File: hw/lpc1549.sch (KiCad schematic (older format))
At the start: 20 parts, among them J301 ARM_JTAG_SWD_HEADER_10_PINSMD, U301 LPC1549JBD64, U302 MCP2551_SOIC8, X301 XTAL_7A-12.000MAAJ-T

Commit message: creating hw 3.0.0
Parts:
- removed R301, R304, R305, R307: 10K, multicomp:0603, symbol 10K
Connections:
- net EMCY: now also U301.P$41 (VBAT)
- net KEY_19: now also U301.P$33 (PIO1_4/ADC1_10)
- net KEY_50: now also U301.P$39 (PIO0_17/WAKEUP/!TRST)
- net KEY_AC: now also U301.P$34 (PIO1_5/ADC1_11)
- net HEATERBAT renamed HEATER
- net HEATERBAT_SENSE: no longer names the net of U301.P$8 (PIO0_4/ADC0_4)
- net HEATERVDD: no longer names the net of U301.P$30 (PIO0_14/ADC1_7/SCT1_OUT5)
- net HEATERVDD_SENSE renamed HEATER_SENSE
- net OUT4: no longer names the net of U301.P$64 (PIO0_29/ACMP2_I3/SCT2_OUT4)
- net OUT4_SENSE: no longer names the net of U301.P$2 (PIO0_0/ADC0_10/SCT0_OUT3)

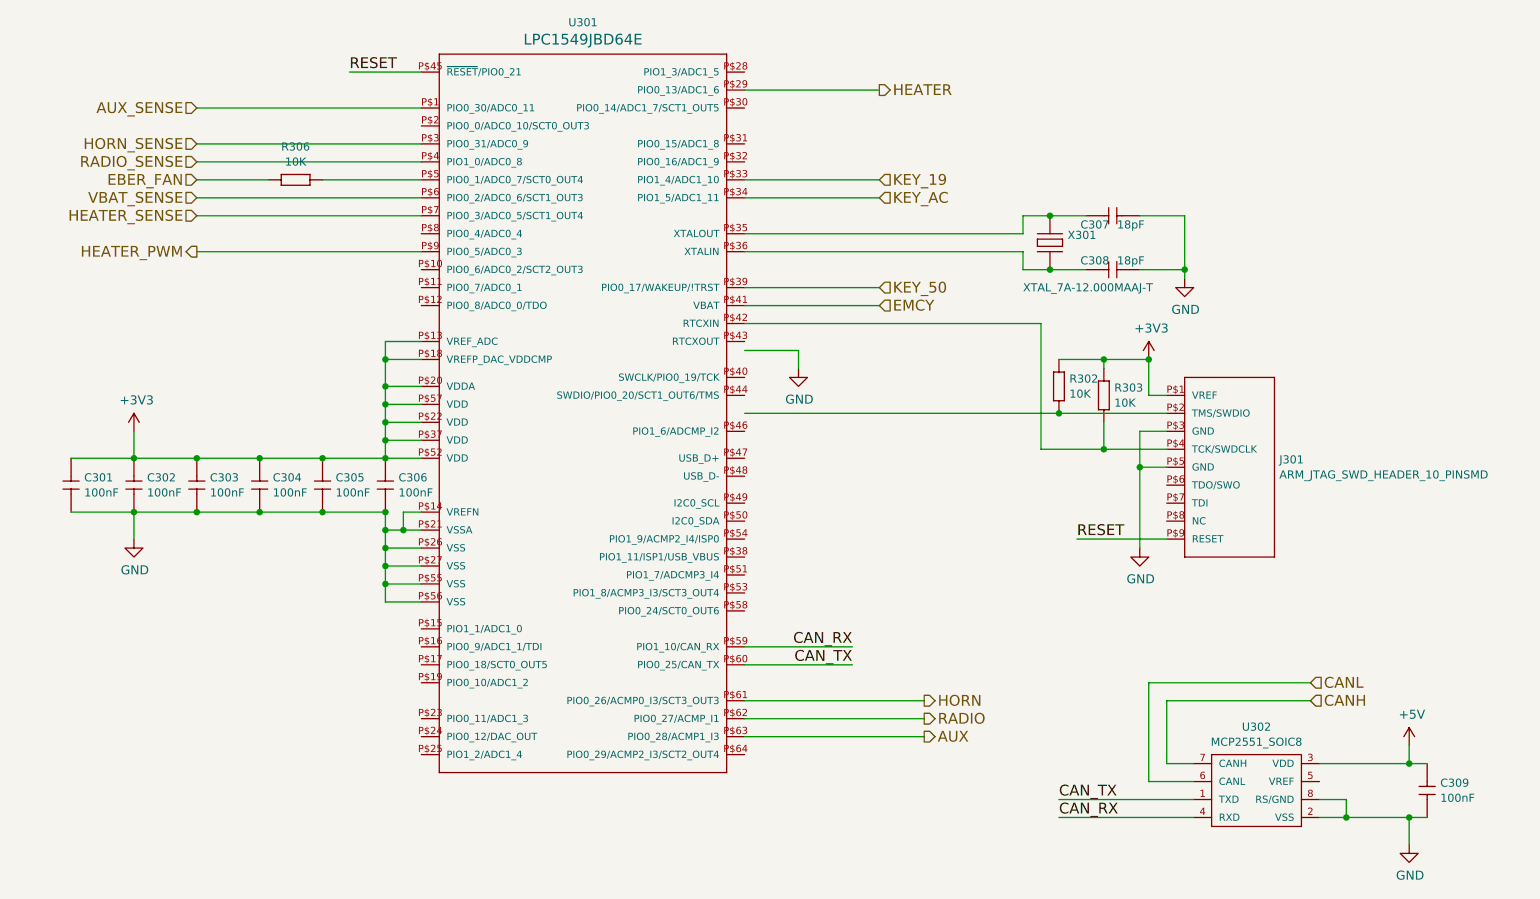
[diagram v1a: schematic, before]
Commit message: key_50 moved out from ISP pin
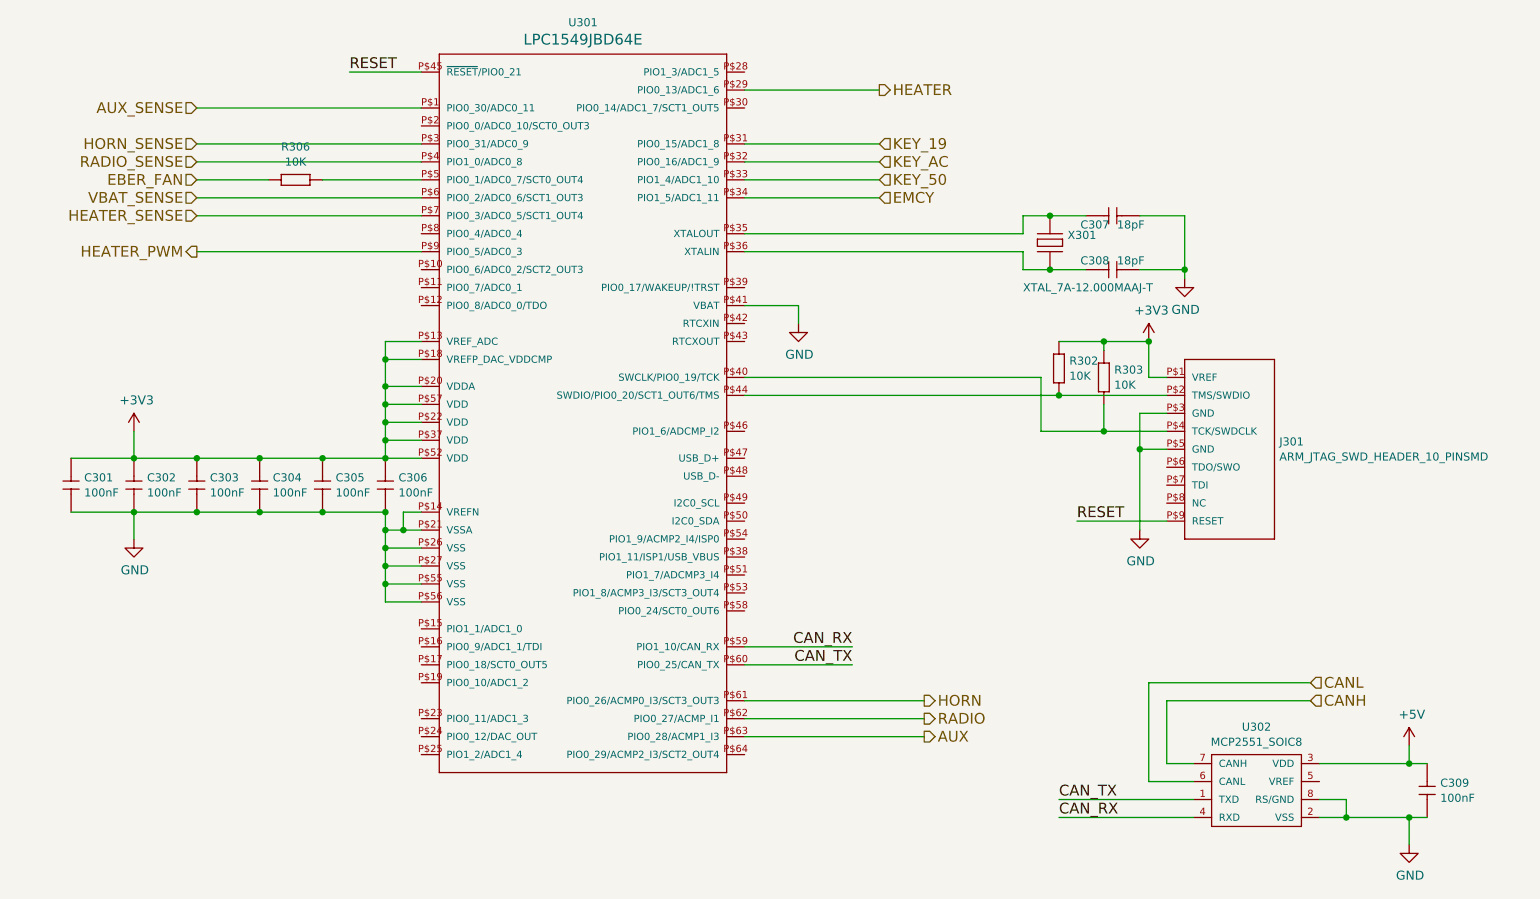
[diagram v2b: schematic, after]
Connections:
- net EMCY: now also U301.P$34 (PIO1_5/ADC1_11); no longer U301.P$41 (VBAT)
- net GND: now also U301.P$41 (VBAT)
- net KEY_19: now also U301.P$31 (PIO0_15/ADC1_8); no longer U301.P$33 (PIO1_4/ADC1_10)
- net KEY_50: now also U301.P$33 (PIO1_4/ADC1_10); no longer U301.P$39 (PIO0_17/WAKEUP/!TRST)
- net KEY_AC: now also U301.P$32 (PIO0_16/ADC1_9); no longer U301.P$34 (PIO1_5/ADC1_11)
- net at J301.P$2 (TMS/SWDIO), R302.1 (R1): now also U301.P$44 (SWDIO/PIO0_20/SCT1_OUT6/TMS)
- net at J301.P$4 (TCK/SWDCLK), R303.1 (R1): now also U301.P$40 (SWCLK/PIO0_19/TCK); no longer U301.P$42 (RTCXIN)
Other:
- moved on the sheet: J301, R302, R303
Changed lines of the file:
@@
 $EndComp
 $Comp
-L +3V3 #PWR301
+L +3V3 #PWR016
 U 1 1 57E689A3
 P 3000 3850
-F 0 "#PWR301" H 3000 3700 50  0001 C CNN
+F 0 "#PWR016" H 3000 3700 50  0001 C CNN
 F 1 "+3V3" H 3015 4023 50  0000 C CNN
 F 2 "" H 3000 3850 50  0000 C CNN
@@
 $EndComp
 $Comp
-L GND #PWR302
+L GND #PWR017
 U 1 1 57E689C9
 P 3000 4450
-F 0 "#PWR302" H 3000 4200 50  0001 C CNN
+F 0 "#PWR017" H 3000 4200 50  0001 C CNN
 F 1 "GND" H 3005 4277 50  0000 C CNN
 F 2 "" H 3000 4450 50  0000 C CNN
@@
 $EndComp
 $Comp
-L GND #PWR306
+L GND #PWR018
 U 1 1 57E697A1
 P 8850 3000
-F 0 "#PWR306" H 8850 2750 50  0001 C CNN
+F 0 "#PWR018" H 8850 2750 50  0001 C CNN
 F 1 "GND" H 8855 2827 50  0000 C CNN
 F 2 "" H 8850 3000 50  0000 C CNN
@@
 $EndComp
 $Comp
-L GND #PWR303
+L GND #PWR019
 U 1 1 57E69A8B
-P 6700 3500
-F 0 "#PWR303" H 6700 3250 50  0001 C CNN
-F 1 "GND" H 6705 3327 50  0000 C CNN
-F 2 "" H 6700 3500 50  0000 C CNN
-F 3 "" H 6700 3500 50  0000 C CNN
-	1    6700 3500
-	1    0    0    -1
-$EndComp
-$Comp
-L GND #PWR304
+P 6700 3250
+F 0 "#PWR019" H 6700 3000 50  0001 C CNN
+F 1 "GND" H 6705 3077 50  0000 C CNN
+F 2 "" H 6700 3250 50  0000 C CNN
+F 3 "" H 6700 3250 50  0000 C CNN
+	1    6700 3250
+	1    0    0    -1
+$EndComp
+$Comp
+L GND #PWR020
 U 1 1 5891FBFB
-P 8600 4500
-F 0 "#PWR304" H 8600 4250 50  0001 C CNN
-F 1 "GND" H 8605 4327 50  0000 C CNN
-F 2 "" H 8600 4500 50  0000 C CNN
-F 3 "" H 8600 4500 50  0000 C CNN
-	1    8600 4500
-	1    0    0    -1
-$EndComp
-$Comp
-L +3V3 #PWR305
+P 8600 4400
+F 0 "#PWR020" H 8600 4150 50  0001 C CNN
+F 1 "GND" H 8605 4227 50  0000 C CNN
+F 2 "" H 8600 4400 50  0000 C CNN
+F 3 "" H 8600 4400 50  0000 C CNN
+	1    8600 4400
+	1    0    0    -1
+$EndComp
+$Comp
+L +3V3 #PWR021
 U 1 1 5891FCDE
-P 8650 3450
-F 0 "#PWR305" H 8650 3300 50  0001 C CNN
-F 1 "+3V3" H 8665 3623 50  0000 C CNN
-F 2 "" H 8650 3450 50  0000 C CNN
-F 3 "" H 8650 3450 50  0000 C CNN
-	1    8650 3450
-	1    0    0    -1
-$EndComp
-Text Label 8250 4450 0    60   ~ 0
+P 8650 3350
+F 0 "#PWR021" H 8650 3200 50  0001 C CNN
+F 1 "+3V3" H 8665 3523 50  0000 C CNN
+F 2 "" H 8650 3350 50  0000 C CNN
+F 3 "" H 8650 3350 50  0000 C CNN
+	1    8650 3350
+	1    0    0    -1
+$EndComp
+Text Label 8250 4350 0    60   ~ 0
 RESET
 Text Label 4200 1850 0    60   ~ 0
@@
 L 10K R302
 U 1 1 589226EB
-P 8150 3550
-F 0 "R302" V 8158 3608 45  0000 L CNN
-F 1 "10K" V 8242 3608 45  0000 L CNN
-F 2 "multicomp:0603" H 8180 3700 20  0001 C CNN
-F 3 "http://www.farnell.com/datasheets/1788326.pdf?_ga=1.214208087.1948984246.1460023966" H 8119 3589 60  0001 C CNN
-F 4 "9330399" H 8519 3989 60  0001 C CNN "1st Source Part Number"
-F 5 "Farnell" H 8419 3889 60  0001 C CNN "1st Source"
-F 6 "MC0063W0603110K" H 8319 3789 60  0001 C CNN "Manufacturer Part Number"
-F 7 "MULTICOMP" H 8219 3689 60  0001 C CNN "Manufacturer"
-	1    8150 3550
+P 8150 3450
+F 0 "R302" V 8158 3508 45  0000 L CNN
+F 1 "10K" V 8242 3508 45  0000 L CNN
+F 2 "multicomp:0603" H 8180 3600 20  0001 C CNN
+F 3 "http://www.farnell.com/datasheets/1788326.pdf?_ga=1.214208087.1948984246.1460023966" H 8119 3489 60  0001 C CNN
+F 4 "9330399" H 8519 3889 60  0001 C CNN "1st Source Part Number"
+F 5 "Farnell" H 8419 3789 60  0001 C CNN "1st Source"
+F 6 "MC0063W0603110K" H 8319 3689 60  0001 C CNN "Manufacturer Part Number"
+F 7 "MULTICOMP" H 8219 3589 60  0001 C CNN "Manufacturer"
+	1    8150 3450
 	0    1    1    0
 $EndComp
@@
 L 10K R303
 U 1 1 58922760
-P 8400 3600
-F 0 "R303" V 8408 3658 45  0000 L CNN
-F 1 "10K" V 8492 3658 45  0000 L CNN
-F 2 "multicomp:0603" H 8430 3750 20  0001 C CNN
-F 3 "http://www.farnell.com/datasheets/1788326.pdf?_ga=1.214208087.1948984246.1460023966" H 8369 3639 60  0001 C CNN
-F 4 "9330399" H 8769 4039 60  0001 C CNN "1st Source Part Number"
-F 5 "Farnell" H 8669 3939 60  0001 C CNN "1st Source"
-F 6 "MC0063W0603110K" H 8569 3839 60  0001 C CNN "Manufacturer Part Number"
-F 7 "MULTICOMP" H 8469 3739 60  0001 C CNN "Manufacturer"
-	1    8400 3600
+P 8400 3500
+F 0 "R303" V 8408 3558 45  0000 L CNN
+F 1 "10K" V 8492 3558 45  0000 L CNN
+F 2 "multicomp:0603" H 8430 3650 20  0001 C CNN
+F 3 "http://www.farnell.com/datasheets/1788326.pdf?_ga=1.214208087.1948984246.1460023966" H 8369 3539 60  0001 C CNN
+F 4 "9330399" H 8769 3939 60  0001 C CNN "1st Source Part Number"
+F 5 "Farnell" H 8669 3839 60  0001 C CNN "1st Source"
+F 6 "MC0063W0603110K" H 8569 3739 60  0001 C CNN "Manufacturer Part Number"
+F 7 "MULTICOMP" H 8469 3639 60  0001 C CNN "Manufacturer"
+	1    8400 3500
 	0    1    1    0
 $EndComp
 $Comp
-L GND #PWR308
+L GND #PWR022
 U 1 1 58C01588
 P 10100 6150
-F 0 "#PWR308" H 10100 5900 50  0001 C CNN
+F 0 "#PWR022" H 10100 5900 50  0001 C CNN
 F 1 "GND" H 10105 5977 50  0000 C CNN
 F 2 "" H 10100 6150 50  0000 C CNN
@@
 L ARM_JTAG_SWD_HEADER_10_PINSMD J301
 U 1 1 5953ECE3
-P 8850 3950
-F 0 "J301" H 9377 3892 45  0000 L CNN
-F 1 "ARM_JTAG_SWD_HEADER_10_PINSMD" H 9377 3808 45  0000 L CNN
-F 2 "usevolt:ARM_10_PIN_JTAG_SWD_CONNECTOR" H 8880 4100 20  0001 C CNN
-F 3 "http://portal.fciconnect.com/Comergent//fci/drawing/20021121.pdf" H 8850 4390 60  0001 C CNN
-F 4 "20021121-00010C4LF" H 9050 4590 60  0001 C CNN "Manufacturer Part Number"
-F 5 "609-3695-1-ND" H 9250 4790 60  0001 C CNN "1st Source Part Number"
-F 6 "Amphenol FCI" H 8950 4490 60  0001 C CNN "Manufacturer"
-F 7 "Digikey" H 9150 4690 60  0001 C CNN "1st Source"
-	1    8850 3950
+P 8850 3850
+F 0 "J301" H 9377 3792 45  0000 L CNN
+F 1 "ARM_JTAG_SWD_HEADER_10_PINSMD" H 9377 3708 45  0000 L CNN
+F 2 "usevolt:ARM_10_PIN_JTAG_SWD_CONNECTOR" H 8880 4000 20  0001 C CNN
+F 3 "http://portal.fciconnect.com/Comergent//fci/drawing/20021121.pdf" H 8850 4290 60  0001 C CNN
+F 4 "20021121-00010C4LF" H 9050 4490 60  0001 C CNN "Manufacturer Part Number"
+F 5 "609-3695-1-ND" H 9250 4690 60  0001 C CNN "1st Source Part Number"
+F 6 "Amphenol FCI" H 8950 4390 60  0001 C CNN "Manufacturer"
+F 7 "Digikey" H 9150 4590 60  0001 C CNN "1st Source"
+	1    8850 3850
 	1    0    0    -1
 $EndComp
@@
 $EndComp
 $Comp
-L +5V #PWR307
+L +5V #PWR023
 U 1 1 595E0BE4
 P 10100 5600
-F 0 "#PWR307" H 10100 5450 50  0001 C CNN
+F 0 "#PWR023" H 10100 5450 50  0001 C CNN
 F 1 "+5V" H 10115 5773 50  0000 C CNN
 F 2 "" H 10100 5600 50  0000 C CNN
@@
 Text HLabel 3350 2850 0    60   Output ~ 0
 HEATER_PWM
+Text HLabel 7150 2250 2    60   Input ~ 0
+KEY_19
 Text HLabel 7150 2450 2    60   Input ~ 0
-KEY_19
-Text HLabel 7150 3050 2    60   Input ~ 0
 KEY_50
+Text HLabel 7150 2350 2    60   Input ~ 0
+KEY_AC
 Text HLabel 7150 2550 2    60   Input ~ 0
-KEY_AC
-Text HLabel 7150 3150 2    60   Input ~ 0
 EMCY
 Text HLabel 3350 2650 0    60   Input ~ 0
@@
 Connection ~ 8850 2950
 Wire Wire Line
-	6700 3500 6700 3400
-Wire Wire Line
-	6700 3400 6400 3400
+	6700 3250 6700 3150
+Wire Wire Line
+	6700 3150 6400 3150
 Wire Wire Line
 	6400 5150 7000 5150
@@
 	7000 5050 6400 5050
 Wire Wire Line
-	6400 3250 8050 3250
-Wire Wire Line
-	8050 3250 8050 3950
-Wire Wire Line
-	8050 3950 8750 3950
-Wire Wire Line
-	6400 3750 8750 3750
-Wire Wire Line
-	8600 3850 8600 4500
-Wire Wire Line
-	8600 4050 8750 4050
-Wire Wire Line
-	8600 3850 8750 3850
-Connection ~ 8600 4050
-Wire Wire Line
-	8650 3450 8650 3650
-Wire Wire Line
-	8650 3650 8750 3650
-Wire Wire Line
-	8750 4450 8250 4450
+	8050 3850 8750 3850
+Wire Wire Line
+	6400 3650 8750 3650
+Wire Wire Line
+	8600 3750 8600 4400
+Wire Wire Line
+	8600 3950 8750 3950
+Wire Wire Line
+	8600 3750 8750 3750
+Connection ~ 8600 3950
+Wire Wire Line
+	8650 3350 8650 3550
+Wire Wire Line
+	8650 3550 8750 3550
+Wire Wire Line
+	8750 4350 8250 4350
 Wire Wire Line
 	4600 1850 4200 1850
-Connection ~ 8150 3750
-Wire Wire Line
-	8400 3800 8400 3950
-Connection ~ 8400 3950
-Wire Wire Line
-	8150 3450 8650 3450
-Wire Wire Line
-	8400 3500 8400 3450
-Connection ~ 8400 3450
-Connection ~ 8650 3450
+Connection ~ 8150 3650
+Wire Wire Line
+	8400 3700 8400 3850
+Connection ~ 8400 3850
+Wire Wire Line
+	8150 3350 8650 3350
+Wire Wire Line
+	8400 3400 8400 3350
+Connection ~ 8400 3350
+Connection ~ 8650 3350
 Wire Wire Line
 	9600 6000 10200 6000
@@
 	3350 2850 4600 2850
 Wire Wire Line
+	6400 2350 7150 2350
+Wire Wire Line
+	6400 2450 7150 2450
+Wire Wire Line
+	6400 2250 7150 2250
+Wire Wire Line
 	6400 2550 7150 2550
 Wire Wire Line
-	6400 3050 7150 3050
-Wire Wire Line
-	6400 2450 7150 2450
-Wire Wire Line
-	6400 3150 7150 3150
-Wire Wire Line
 	4600 2650 3350 2650
 Wire Wire Line
 	4600 2550 3350 2550
+Wire Wire Line
+	8050 3850 8050 3550
+Wire Wire Line
+	8050 3550 6400 3550
 $EndSCHEMATC
